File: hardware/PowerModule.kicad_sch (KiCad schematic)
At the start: 11 parts, among them U7 LM1117-3.3, U8 LM1117-3.3, U9 LM1117-3.3

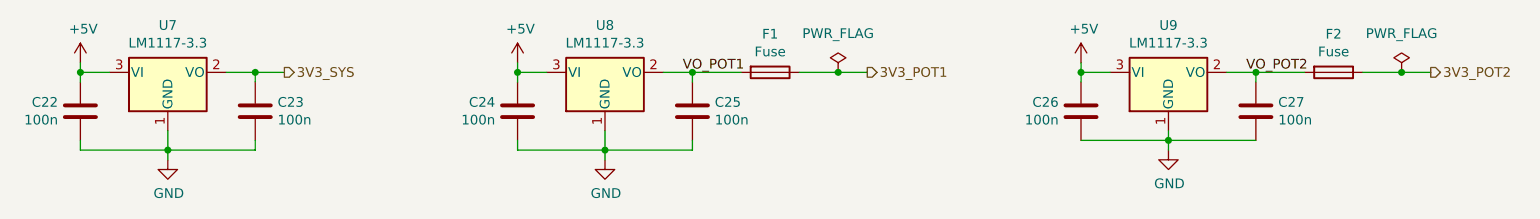
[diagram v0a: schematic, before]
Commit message: Add brake pressure sensors
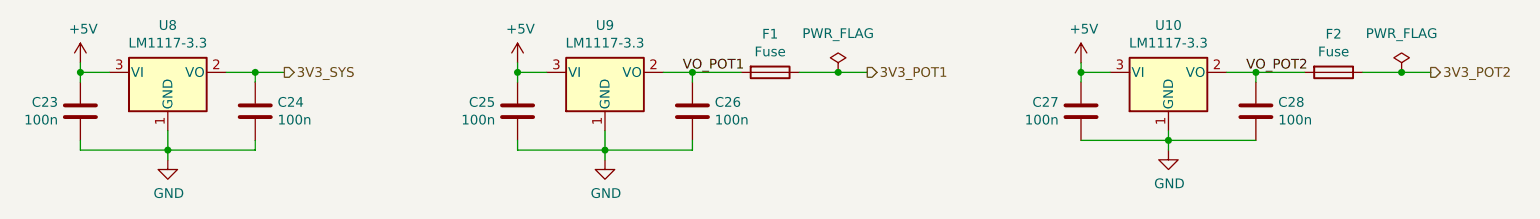
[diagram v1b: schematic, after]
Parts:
- renumbered C22 to C23, C23 to C24, C24 to C25, C25 to C26, C26 to C27, C27 to C28, U9 to U10, U7 to U8, U8 to U9
